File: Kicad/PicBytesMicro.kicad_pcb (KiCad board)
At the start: 2 copper layers, 80 x 125 mm, 274 parts, among them IC1 FS312F-G, Q1 SMMBT5551LT1G, Q10 SMMBT5551LT1G, Q11 SMMBT5551LT1G, Q12 SMMBT5551LT1G, Q13 SMMBT5551LT1G, Q14 SMMBT5551LT1G, Q15 SMMBT5551LT1G, Q16 SMMBT5551LT1G, Q17 SMMBT5551LT1G, Q18 SMMBT5551LT1G, Q19 SMMBT5551LT1G, Q2 SMMBT5551LT1G, Q20 SMMBT5551LT1G, Q21 SMMBT5551LT1G, Q22 SMMBT5551LT1G, Q23 SMMBT5551LT1G, Q24 SMMBT5551LT1G, Q25 SMMBT5551LT1G, Q26 SMMBT5551LT1G, Q27 SMMBT5551LT1G, Q28 SMMBT5551LT1G, Q29 SMMBT5551LT1G, Q3 SMMBT5551LT1G, Q30 FS8205, Q4 SMMBT5551LT1G, Q5 SMMBT5551LT1G, Q6 SMMBT5551LT1G, Q7 SMMBT5551LT1G, Q8 SMMBT5551LT1G, Q9 SMMBT5551LT1G

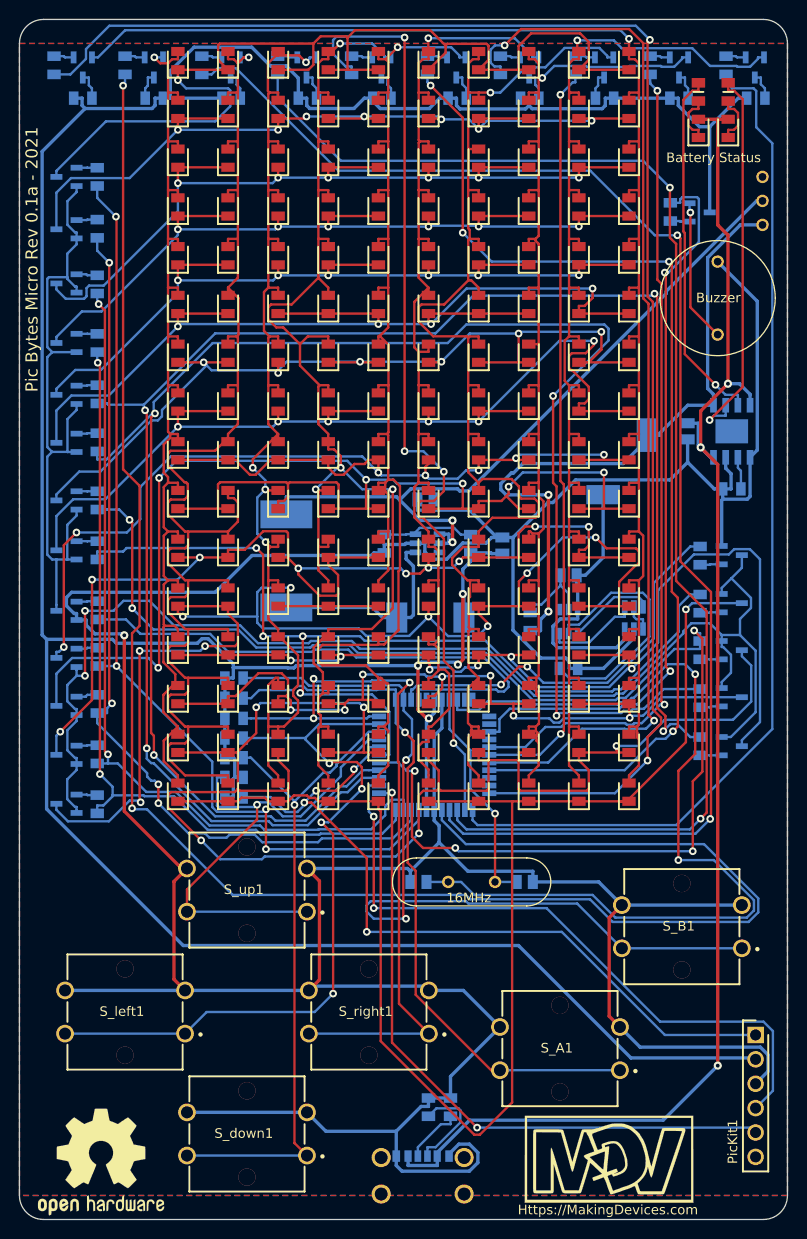
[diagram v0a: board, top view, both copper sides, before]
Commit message: New V1.2 Hardware Release
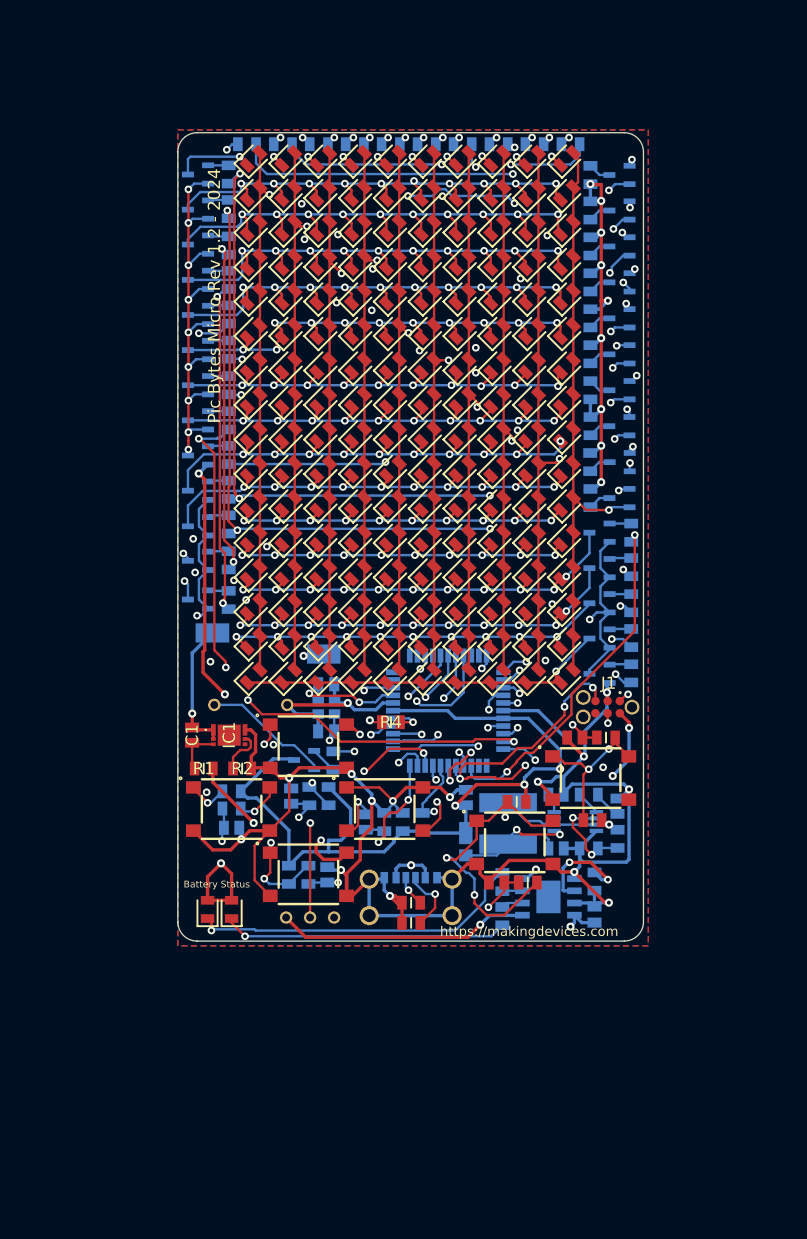
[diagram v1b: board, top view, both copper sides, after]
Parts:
- removed 16MhzCrystal1: AS-16.000MAHK-B, SamacSys_Parts:AS16000MAHKB
- removed C_0.1u_1, C_22u_1, C_22u_2: GCG21BR71H154KA01K, SamacSys_Parts:CAPC2012X145N
- removed D_1: SS34-E3_57T, SamacSys_Parts:DIOM7959X262N
- removed G***: LOGO, MDV:logo_MDV_2
- removed L_22uH_1: SRR1260-220M, SamacSys_Parts:SRR1260-150M
- removed PicKit1: M20-9990645, SamacSys_Parts:HDRV6W66P0X254_1X6_1524X254X874P
- removed Q30: FS8205, SamacSys_Parts:FS8205
- removed REF**: OSHW-Logo2_14.6x12mm_SilkScreen, Symbol:OSHW-Logo2_14.6x12mm_SilkScreen
- removed R_100_1, R_1k_3, R_2k_2, R_7.5k_1: KTR10EZPF4220, SamacSys_Parts:RESC2012X65N
- removed S_A1, S_B1: B3F-4050, SamacSys_Parts:B3F-4000
- removed U_StepUp1: MT3608, SamacSys_Parts:SOT95P280X145-6N
- added C1: 1uF, SamacSys_Parts:CAPC2012X140N, F.Cu at (114.5, 109.0)
- added C2: 820pF, User_lib:CAPC2012X140N, B.Cu at (158.8, 116.5)
- added C3: 22uF, User_lib:CAPC2012X140N, B.Cu at (152.4, 120.8)
- added C4: 100nF, User_lib:CAPC2012X140N, B.Cu at (152.4, 115.2)
- added C5: 47uF, User_lib:CAPC2012X140N, B.Cu at (143.0, 115.5)
- added C_100F_1: GCG21BR71H154KA01K, User_lib:CAPC2012X140N, B.Cu at (124.8, 115.4)
- added C_22p_3: GCG21BR71H154KA01K, User_lib:CAPC2012X140N, B.Cu at (118.6, 118.7)
- added C_22p_4: GCG21BR71H154KA01K, User_lib:CAPC2012X140N, B.Cu at (128.6, 123.6)
- added C_22p_5: GCG21BR71H154KA01K, User_lib:CAPC2012X140N, B.Cu at (132.6, 118.1)
- added C_22p_6: GCG21BR71H154KA01K, User_lib:CAPC2012X140N, F.Cu at (154.3, 109.3)
- added C_22p_7: GCG21BR71H154KA01K, User_lib:CAPC2012X140N, F.Cu at (146.2, 124.4)
- added D1: FSV360FP, User_lib:SS12FP, B.Cu at (143.0, 120.2)
- added IC2: TPS61085TDGKR, User_lib:SOP65P490X110-8N, B.Cu at (154.4, 118.0)
- added J1: TC2030-MCP-NL, User_lib:TC2030-MCP-NL, F.Cu at (157.8, 106.1)
- added L1: 4.7uH, User_lib:SRN6045_1, B.Cu at (147.4, 118.2)
- added R1: 330, SamacSys_Parts:RESC2012X75N, F.Cu at (115.7, 112.5)
- added R2: 2.7k, SamacSys_Parts:RESC2012X75N, F.Cu at (119.7, 112.5)
- added R3: 44.2k, User_lib:RESC2012X75N, B.Cu at (155.8, 115.2)
- added R4: 10k, SamacSys_Parts:RESC2012X75N, F.Cu at (135.2, 107.7)
- added R5: 82k, User_lib:RESC2012X75N, B.Cu at (158.8, 119.8)
- added R6: 27k, User_lib:RESC2012X75N, B.Cu at (155.8, 120.8)
- added R_10K_10: KTR10EZPF4220, User_lib:RESC2012X75N, F.Cu at (157.6, 109.3)
- added R_10K_11: KTR10EZPF4220, User_lib:RESC2012X75N, F.Cu at (149.4, 124.4)
- added R_10K_2: KTR10EZPF4220, User_lib:RESC2012X75N, B.Cu at (118.6, 116.7)
- added R_10K_4: KTR10EZPF4220, User_lib:RESC2012X75N, B.Cu at (126.6, 123.6)
- added R_10K_5: KTR10EZPF4220, User_lib:RESC2012X75N, B.Cu at (128.7, 115.4)
- added R_10K_8: KTR10EZPF4220, User_lib:RESC2012X75N, B.Cu at (134.5, 118.1)
- added S_a1: 430182050816, User_lib:430182070816, F.Cu at (148.1, 120.2)
- added S_b1: 430182050816, User_lib:430182070816, F.Cu at (156.0, 113.5)
- added Y1: CX2520DB12000D0GPSC1, User_lib:CX2520DB12000D0GPSC1, B.Cu at (128.5, 106.2)
- IC1: value FS312F-G -> AP9214L-AN-HSBR-7; footprint SamacSys_Parts:SOT95P280X145-6N -> SamacSys_Parts:AP9214LANHSBR7; moved to F.Cu
- LS1, R_1k_1, R_1k_2: moved to B.Cu
- R_10K_12: renamed from R_10K_5; moved to F.Cu
- R_10K_13: renamed from R_10K_6; moved to F.Cu
- R_5.1_1, R_5.1k_1: moved to F.Cu
- S_down1, S_left1, S_right1, S_up1: value B3F-4050 -> 430182050816; footprint SamacSys_Parts:B3F-4000 -> User_lib:430182070816
- moved LED_RED_bms1 96.4 mm to (118.6, 127.2)
- moved LED_Green_bms1 96.1 mm to (116.1, 127.2)
- moved R_1k_1 89.0 mm to (146.8, 127.9)
- moved SW_Toggle1 87.6 mm to (124.3, 128.1), turned to 0 degrees
- moved R_1k_2 84.8 mm to (146.8, 124.3), turned to 90 degrees
- moved Q27 71.7 mm to (159.0, 84.4), turned to 180 degrees
- moved Q1 70.4 mm to (126.2, 111.6), turned to 180 degrees
- moved R220_10 67.3 mm to (156.0, 84.4), turned to -90 degrees
- moved R4K7_1 67.1 mm to (129.2, 111.7)
- moved LS1 65.1 mm to (116.8, 105.9), turned to 90 degrees
- moved R4K7_27 54.4 mm to (153.9, 47.5), turned to 180 degrees
- moved IC_BMS_TP1 52.1 mm to (151.6, 125.9), turned to 180 degrees
- moved C_10u_1 51.3 mm to (156.4, 127.7), turned to 90 degrees
- moved Q4 49.8 mm to (159.0, 50.7), turned to 180 degrees
- moved R220_1 46.1 mm to (156.0, 50.7), turned to 90 degrees
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- renumbered IC_BMS_TP4056 to IC_BMS_TP1, PIC18F45K50 to PIC18F45K1, Q29 to Q1, Q9 to Q10, Q10 to Q11, Q11 to Q12, Q12 to Q13, Q13 to Q14, Q14 to Q15, Q15 to Q16, Q16 to Q17, Q17 to Q18, Q18 to Q19, Q1 to Q2, Q19 to Q20, Q20 to Q21, Q21 to Q22, Q22 to Q23, Q23 to Q24, Q24 to Q25, Q25 to Q26, Q26 to Q27, Q27 to Q28, Q28 to Q29, Q2 to Q3, Q3 to Q4, Q4 to Q5, Q5 to Q6, Q6 to Q7, Q7 to Q8, Q8 to Q9, R4K7_29 to R4K7_1, R4K7_9 to R4K7_10, R4K7_10 to R4K7_11, R4K7_11 to R4K7_12, R4K7_12 to R4K7_13, R4K7_13 to R4K7_14, R4K7_14 to R4K7_15, R4K7_15 to R4K7_16, R4K7_16 to R4K7_17, R4K7_17 to R4K7_18, R4K7_18 to R4K7_19, R4K7_1 to R4K7_2, R4K7_19 to R4K7_20, R4K7_20 to R4K7_21, R4K7_21 to R4K7_22, R4K7_22 to R4K7_23, R4K7_23 to R4K7_24, R4K7_24 to R4K7_25, R4K7_25 to R4K7_26, R4K7_26 to R4K7_27, R4K7_27 to R4K7_28, R4K7_28 to R4K7_29, R4K7_2 to R4K7_3, R4K7_3 to R4K7_4, R4K7_4 to R4K7_5, R4K7_5 to R4K7_6, R4K7_6 to R4K7_7, R4K7_7 to R4K7_8, R4K7_8 to R4K7_9, R_10K_1 to R_10K_3, R_10K_3 to R_10K_6, R_10K_2 to R_10K_7, R_10K_4 to R_10K_9
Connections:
- IC1 pad 1: Net-(IC1-Pad1) -> BAT-
- IC1 pad 2: Net-(IC1-Pad2) -> BAT-
- IC1 pad 4: Net-(IC1-Pad4) -> unconnected-(IC1-NC-Pad4)
- IC1 pad 6: BAT- -> Vgnd_main
- IC_BMS_TP1 pad 9: Net-(IC_BMS_TP4056-Pad9) -> unconnected-(IC_BMS_TP1-EP-Pad9)
- J_USB_C1 pad MH1: Net-(J_USB_C1-PadMH1) -> Vgnd_main
- J_USB_C1 pad MH2: Net-(J_USB_C1-PadMH2) -> Vgnd_main
- J_USB_C1 pad MH3: Net-(J_USB_C1-PadMH3) -> Vgnd_main
- J_USB_C1 pad MH4: Net-(J_USB_C1-PadMH4) -> Vgnd_main
- PIC18F45K1 pad 12: ICSPCLK -> unconnected-(PIC18F45K1-NC/ICCK/ICPGC-Pad12)
- PIC18F45K1 pad 13: ICSPDA -> unconnected-(PIC18F45K1-NC/ICDT/ICPGD-Pad13)
- PIC18F45K1 pad 16: P_CR6 -> ICSPCLK
- PIC18F45K1 pad 17: P_CR7 -> ICSPDA
- PIC18F45K1 pad 27: Net-(PIC18F45K50-Pad27) -> Vdc_battery
- PIC18F45K1 pad 32: Net-(PIC18F45K50-Pad32) -> unconnected-(PIC18F45K1-RC0-Pad32)
- PIC18F45K1 pad 33: Net-(PIC18F45K50-Pad33) -> unconnected-(PIC18F45K1-NC/~{ICRST}/ICVPP-Pad33)
- PIC18F45K1 pad 34: Net-(PIC18F45K50-Pad34) -> unconnected-(PIC18F45K1-NC-Pad34)
- PIC18F45K1 pad 35: Net-(PIC18F45K50-Pad35) -> unconnected-(PIC18F45K1-RC1-Pad35)
- PIC18F45K1 pad 37: Net-(PIC18F45K50-Pad37) -> unconnected-(PIC18F45K1-VUSB3V3-Pad37)
- PIC18F45K1 pad 42: Net-(PIC18F45K50-Pad42) -> unconnected-(PIC18F45K1-D--Pad42)
- PIC18F45K1 pad 43: Net-(PIC18F45K50-Pad43) -> unconnected-(PIC18F45K1-D+-Pad43)
- R4K7_24 pad 1: P_CR6 -> ICSPCLK
- R4K7_25 pad 1: P_CR6 -> ICSPCLK
- R4K7_28 pad 1: P_CR7 -> ICSPDA
- R4K7_29 pad 1: P_CR7 -> ICSPDA
- R_10K_12 pad 1: S_b -> Net-(R_10K_10-Pad2)
- R_10K_13 pad 1: S_a -> Net-(R_10K_11-Pad2)
- R_10K_3 pad 1: S_left -> Net-(R_10K_2-Pad2)
- R_10K_6 pad 1: S_up -> Net-(R_10K_5-Pad1)
- R_10K_6 pad 2: Vcc_main -> S_up
- R_10K_7 pad 1: S_down -> Net-(R_10K_4-Pad2)
- R_10K_9 pad 1: S_right -> Vgnd_main
- SW_Toggle1 pad 3: Net-(SW_Toggle1-Pad3) -> unconnected-(SW_Toggle1-Pad3)
- S_down1 pad 1: S_down -> Net-(R_10K_4-Pad2)
- S_down1 pad 2: S_down -> Vgnd_main
- S_down1 pad 3: Vgnd_main -> Net-(R_10K_4-Pad2)
- S_left1 pad 1: S_left -> Net-(R_10K_2-Pad2)
- S_left1 pad 2: S_left -> Vgnd_main
- S_left1 pad 3: Vgnd_main -> Net-(R_10K_2-Pad2)
- S_right1 pad 1: S_right -> Vgnd_main
- S_right1 pad 2: S_right -> Net-(C_22p_5-Pad2)
- S_right1 pad 4: Vgnd_main -> Net-(C_22p_5-Pad2)
- S_up1 pad 1: S_up -> Net-(R_10K_5-Pad1)
- S_up1 pad 2: S_up -> Vgnd_main
- S_up1 pad 3: Vgnd_main -> Net-(R_10K_5-Pad1)
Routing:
- net Vcc_main: track 360.6 -> 183.0 mm, vias 4 -> 15
- net Vgnd_main: track 425.9 -> 264.1 mm, vias 1 -> 17
- net P_CR6: track 145.7 -> 0.00 mm, vias 6 -> 0
- net R15: track 147.4 -> 38.9 mm
- net P_CR7: track 102.3 -> 0.00 mm, vias 4 -> 0
- net C10: track 162.2 -> 60.8 mm
- net R14: track 153.1 -> 52.6 mm, vias 5 -> 10
- net P_CC1: track 187.0 -> 86.8 mm
- net P_CC10: track 159.6 -> 65.1 mm
- net BMS_Vcc: track 151.8 -> 63.1 mm, vias 3 -> 4
- net R11: track 140.2 -> 56.4 mm, vias 9 -> 12
- net R9: track 138.2 -> 55.8 mm, vias 6 -> 10
- net Net-(PIC18F45K1-RA6): track 95.2 -> 13.7 mm
- net P_CR5: track 184.2 -> 107.7 mm
- net P_CR4: track 179.8 -> 108.7 mm
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- added copper zone on In1.Cu, net Vgnd_main
- added copper zone on In2.Cu, net Vgnd_main
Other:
- board size 80 x 125 mm -> 48.5 x 84.2 mm
- copper layers 2 -> 4
- board text added: "Pic Bytes Micro Rev 1.2 - 2024"
- board text added: "https://makingdevices.com"
- board text removed: "16MHz"
- board text removed: "FS312"
- board text removed: "Https://MakingDevices.com"
- board text removed: "MT3608"
- board text removed: "Pic Bytes Micro Rev 0.1a - 2021"
- board text removed: "R10K"
- board text removed: "R4K7"
- board text removed: "R5K1"
- board text removed: "TP4056"
- board text removed: "Type C"

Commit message: V1.25 FW release
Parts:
- renumbered LED_Green_bms1 to LED_Red_bms1, LED_RED_bms1 to LED_green_bms1
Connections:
- C_22p_5 pad 2: Net-(C_22p_5-Pad2) -> Vgnd_main
- R_10K_8 pad 2: Vgnd_main -> Net-(R_10K_8-Pad2)
- R_10K_9 pad 1: Vgnd_main -> Net-(R_10K_8-Pad2)
- S_right1 pad 1: Vgnd_main -> Net-(R_10K_8-Pad2)
- S_right1 pad 2: Net-(C_22p_5-Pad2) -> Vgnd_main
- S_right1 pad 3: Vgnd_main -> Net-(R_10K_8-Pad2)
- S_right1 pad 4: Net-(C_22p_5-Pad2) -> Vgnd_main
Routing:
- net Net-(C_22p_5-Pad2): track 17.9 -> 0.00 mm, vias 2 -> 0
- net Net-(R_10K_8-Pad2): track 0.00 -> 14.3 mm, vias 0 -> 1
- net Vgnd_main: track 264.1 -> 250.3 mm

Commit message: New HW v1.25 release
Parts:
- IC1: value AP9214L-AN-HSBR-7 -> AP9214L-AD-HSBR-7
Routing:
- net Vgnd_main: track 250.3 -> 250.9 mm
- net S_down: track 24.7 -> 25.2 mm
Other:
- board text added: "Pic Bytes Micro Rev 1.25 - 2024"
- board text removed: "Pic Bytes Micro Rev 1.2 - 2024"
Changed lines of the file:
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@@
         (effects (font (size 1.27 1.27) (thickness 0.254)))
     )
-    (fp_text value "AP9214L-AN-HSBR-7" (at 3.475 2 90) (layer "F.SilkS") hide
+    (fp_text value "AP9214L-AD-HSBR-7" (at 3.475 2 90) (layer "F.SilkS") hide
         (effects (font (size 1.27 1.27) (thickness 0.254)))
     )
@@
     (property "ki_description" "Power Inductor semi-shielded SMD 4.7uH Bourns SRN6045 Series Shielded Wire-wound SMD Inductor with a Ferrite Core, 4.7 uH +/-30% 4A Idc")
     (attr smd)
-    (fp_text reference "L1" (at -0.327 0.037 90) (layer "B.SilkS")
+    (fp_text reference "L1" (at -0.327 0.037 90) (layer "B.SilkS") hide
         (effects (font (size 1.27 1.27) (thickness 0.254)) (justify mirror))
     )
@@
     (property "ki_description" "Cap Ceramic 4.7uF 10V X7R 20% Pad SMD 0805 125C T/R")
     (attr smd)
-    (fp_text reference "C5" (at 0 0 -270) (layer "B.SilkS")
+    (fp_text reference "C5" (at 0 0 -270) (layer "B.SilkS") hide
         (effects (font (size 1.27 1.27) (thickness 0.254)) (justify mirror))
     )
@@
     (property "ki_description" "Schottky Diodes & Rectifiers 60V 3A Schottky Barrier Rectifier")
     (attr smd)
-    (fp_text reference "D1" (at -0.225 0 -270) (layer "B.SilkS")
+    (fp_text reference "D1" (at -0.225 0 -270) (layer "B.SilkS") hide
         (effects (font (size 1.27 1.27) (thickness 0.254)) (justify mirror))
     )
@@
     (property "ki_description" "Crystals AEC-Q200 12MHz 8pF 2.5x2mm")
     (attr smd)
-    (fp_text reference "Y1" (at -0.225 0) (layer "B.SilkS")
+    (fp_text reference "Y1" (at -0.225 0) (layer "B.SilkS") hide
         (effects (font (size 1.27 1.27) (thickness 0.254)) (justify mirror))
     )
@@
     (effects (font (size 1 1) (thickness 0.25)))
   )
-  (gr_text "Pic Bytes Micro Rev 1.2 - 2024" (at 116.8 63.3 90) (layer "F.SilkS")
+  (gr_text "Pic Bytes Micro Rev 1.25 - 2024" (at 116.8 63.3 90) (layer "F.SilkS")
     (effects (font (size 1.27 1.27) (thickness 0.15)))
   )
@@
   (segment (start 121 120.575) (end 122.575 119) (width 0.25) (layer "F.Cu") (net 5))
   (segment (start 145.4 124.4) (end 144.478618 123.478618) (width 0.35) (layer "F.Cu") (net 5))
+  (segment (start 140.325 117.675) (end 140.7 117.3) (width 0.35) (layer "F.Cu") (net 5))
   (segment (start 130 123.1) (end 130.575 123.675) (width 0.35) (layer "F.Cu") (net 5))
   (segment (start 147.515 122.1) (end 145.4 124.215) (width 0.35) (layer "F.Cu") (net 5))
@@
   (segment (start 140.325 117.7) (end 139.025 119) (width 0.25) (layer "F.Cu") (net 5))
   (segment (start 130.575 125.79273) (end 131.18727 125.79273) (width 0.35) (layer "F.Cu") (net 5))
+  (segment (start 140.7 117.3) (end 140.7 116.7) (width 0.35) (layer "F.Cu") (net 5))
   (segment (start 135.65 125.8) (end 136.35 126.5) (width 0.35) (layer "F.Cu") (net 5))
-  (segment (start 140.325 116.325) (end 140.325 117.7) (width 0.25) (layer "F.Cu") (net 5))
   (segment (start 136.35 127.05) (end 135.1 125.8) (width 0.35) (layer "F.Cu") (net 5))
   (segment (start 153.55 109.525) (end 155.296365 111.271365) (width 0.35) (layer "F.Cu") (net 5))
+  (segment (start 140.7 116.7) (end 140.325 116.325) (width 0.35) (layer "F.Cu") (net 5))
   (segment (start 122.625 112.45) (end 120.725 112.45) (width 0.35) (layer "F.Cu") (net 5))
   (segment (start 154.3 123.3) (end 157.5 126.5) (width 0.35) (layer "F.Cu") (net 5))
@@
   (segment (start 160 115.74643) (end 159.975065 115.771365) (width 0.35) (layer "F.Cu") (net 5))
   (segment (start 120.6 108.5) (end 120 108.5) (width 0.35) (layer "F.Cu") (net 5))
+  (segment (start 140.325 117.7) (end 140.325 117.675) (width 0.35) (layer "F.Cu") (net 5))
   (segment (start 115.1755 81.8) (end 115.8 82.4245) (width 0.35) (layer "F.Cu") (net 5))
   (segment (start 130.575 125) (end 130.575 125.79273) (width 0.35) (layer "F.Cu") (net 5))
@@
   (segment (start 124.6 106.1) (end 124.4 105.9) (width 0.35) (layer "In1.Cu") (net 5))
   (segment (start 123.125 104.625) (end 124.4 105.9) (width 0.35) (layer "In2.Cu") (net 5))
+  (segment (start 132.6255 115.15) (end 131.7755 116) (width 0.35) (layer "In2.Cu") (net 5))
+  (segment (start 132.9755 114.8) (end 132.6255 115.15) (width 0.35) (layer "In2.Cu") (net 5))
+  (segment (start 139.15 115.15) (end 140 116) (width 0.35) (layer "In2.Cu") (net 5))
   (segment (start 117.9 104.8) (end 118.075 104.625) (width 0.35) (layer "In2.Cu") (net 5))
-  (segment (start 139.15 115.15) (end 140 116) (width 0.25) (layer "In2.Cu") (net 5))
-  (segment (start 131.7755 116) (end 132.6255 115.15) (width 0.25) (layer "In2.Cu") (net 5))
-  (segment (start 132.6255 115.15) (end 139.15 115.15) (width 0.25) (layer "In2.Cu") (net 5))
+  (segment (start 138.8 114.8) (end 132.9755 114.8) (width 0.35) (layer "In2.Cu") (net 5))
+  (segment (start 139.15 115.15) (end 138.8 114.8) (width 0.35) (layer "In2.Cu") (net 5))
   (segment (start 118.075 104.625) (end 123.125 104.625) (width 0.35) (layer "In2.Cu") (net 5))
   (segment (start 119.6 119.9) (end 119.6 118.7) (width 0.35) (layer "B.Cu") (net 5))
@@
   (via (at 129.7 124.4) (size 0.8) (drill 0.4) (layers "F.Cu" "B.Cu") (net 70))
   (via (at 138.602551 110.911981) (size 0.8) (drill 0.4) (layers "F.Cu" "B.Cu") (net 70))
-  (segment (start 129.760661 124.4) (end 129.7 124.4) (width 0.25) (layer "In1.Cu") (net 70))
-  (segment (start 132.4 112.8) (end 132.4 121.760661) (width 0.25) (layer "In1.Cu") (net 70))
-  (segment (start 132.4 121.760661) (end 129.760661 124.4) (width 0.25) (layer "In1.Cu") (net 70))
+  (segment (start 129.760661 124.4) (end 132.5005 121.660161) (width 0.25) (layer "In1.Cu") (net 70))
+  (segment (start 133.1 118.7) (end 133.1 113.5) (width 0.25) (layer "In1.Cu") (net 70))
+  (segment (start 133.1 113.5) (end 132.4 112.8) (width 0.25) (layer "In1.Cu") (net 70))
+  (segment (start 129.7 124.4) (end 129.760661 124.4) (width 0.25) (layer "In1.Cu") (net 70))
+  (segment (start 132.5005 121.660161) (end 132.5005 119.2995) (width 0.25) (layer "In1.Cu") (net 70))
+  (segment (start 132.5005 119.2995) (end 133.1 118.7) (width 0.25) (layer "In1.Cu") (net 70))
   (segment (start 126.75 124.4) (end 126.6 124.55) (width 0.25) (layer "B.Cu") (net 70))
   (segment (start 129.7 124.4) (end 128.57 124.4) (width 0.25) (layer "B.Cu") (net 70))
@@
   (via (at 125.6 117.6) (size 0.8) (drill 0.4) (layers "F.Cu" "B.Cu") (net 71))
   (via (at 139.9 113.7) (size 0.8) (drill 0.4) (layers "F.Cu" "B.Cu") (net 71))
-  (segment (start 139.9 113.7) (end 139 114.6) (width 0.25) (layer "In2.Cu") (net 71))
-  (segment (start 127.8 114.6) (end 125.6 116.8) (width 0.25) (layer "In2.Cu") (net 71))
-  (segment (start 139 114.6) (end 127.8 114.6) (width 0.25) (layer "In2.Cu") (net 71))
-  (segment (start 125.6 116.8) (end 125.6 117.6) (width 0.25) (layer "In2.Cu") (net 71))
+  (segment (start 125.6 116.8) (end 128.1 114.3) (width 0.25) (layer "In2.Cu") (net 71))
+  (segment (start 139.9 113.7) (end 139.35 114.25) (width 0.25) (layer "In2.Cu") (net 71))
+  (segment (start 139.3 114.3) (end 139.35 114.25) (width 0.25) (layer "In2.Cu") (net 71))
+  (segment (start 125.6 117.6) (end 125.6 116.8) (width 0.25) (layer "In2.Cu") (net 71))
+  (segment (start 128.1 114.3) (end 139.3 114.3) (width 0.25) (layer "In2.Cu") (net 71))
   (segment (start 139.562 113.362) (end 139.9 113.7) (width 0.25) (layer "B.Cu") (net 71))
   (segment (start 126.55 116.2) (end 126.7 116.35) (width 0.25) (layer "B.Cu") (net 71))

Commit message: Bill Of Materials
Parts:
- C10: renamed from C_22p_6; value GCG21BR71H154KA01K -> 100nF
- C11: renamed from C_22p_7; value GCG21BR71H154KA01K -> 100nF
- C12: renamed from C_22p_1; value GCG21BR71H154KA01K -> 22pF
- C13: renamed from C_22p_2; value GCG21BR71H154KA01K -> 22pF
- C14: renamed from C_10u_1; value GCG21BR71H154KA01K -> 10uF
- C6: renamed from C_22p_3; value GCG21BR71H154KA01K -> 100nF
- C7: renamed from C_22p_4; value GCG21BR71H154KA01K -> 100nF
- C8: renamed from C_100F_1; value GCG21BR71H154KA01K -> 100nF
- C9: renamed from C_22p_5; value GCG21BR71H154KA01K -> 100nF
- PIC18F4550: renamed from PIC18F45K1; value PIC18F45K50-I_PT -> PIC18F4550-I_PT
- R10: renamed from R4K7_4; value KTR10EZPF4220 -> 4k7
- R11: renamed from R4K7_5; value KTR10EZPF4220 -> 4k7
- R12: renamed from R4K7_6; value KTR10EZPF4220 -> 4k7
- R13: renamed from R4K7_7; value KTR10EZPF4220 -> 4k7
- R14: renamed from R220_1; value KTR10EZPF4220 -> 220
- R15: renamed from R220_2; value KTR10EZPF4220 -> 220
- R16: renamed from R4K7_8; value KTR10EZPF4220 -> 4k7
- R17: renamed from R4K7_9; value KTR10EZPF4220 -> 4k7
- R18: renamed from R4K7_10; value KTR10EZPF4220 -> 4k7
- R19: renamed from R4K7_11; value KTR10EZPF4220 -> 4k7
- R20: renamed from R220_3; value KTR10EZPF4220 -> 220
- R21: renamed from R220_4; value KTR10EZPF4220 -> 220
- R22: renamed from R4K7_12; value KTR10EZPF4220 -> 4k7
- R220: renamed from R220_8; value KTR10EZPF4220 -> 220
- R23: renamed from R4K7_13; value KTR10EZPF4220 -> 4k7
- R24: renamed from R4K7_14; value KTR10EZPF4220 -> 4k7
- R25: renamed from R4K7_15; value KTR10EZPF4220 -> 4k7
- R26: renamed from R4K7_16; value KTR10EZPF4220 -> 4k7
- R27: renamed from R4K7_17; value KTR10EZPF4220 -> 4k7
- R28: renamed from R4K7_18; value KTR10EZPF4220 -> 4k7
- R29: renamed from R4K7_19; value KTR10EZPF4220 -> 4k7
- R30: renamed from R220_5; value KTR10EZPF4220 -> 220
- R31: renamed from R220_6; value KTR10EZPF4220 -> 220
- R32: renamed from R4K7_20; value KTR10EZPF4220 -> 4k7
- R33: renamed from R4K7_21; value KTR10EZPF4220 -> 4k7
- R34: renamed from R4K7_22; value KTR10EZPF4220 -> 4k7
- R35: renamed from R4K7_23; value KTR10EZPF4220 -> 4k7
- R36: renamed from R220_7; value KTR10EZPF4220 -> 220
- R37: renamed from R4K7_24; value KTR10EZPF4220 -> 4k7
- R38: renamed from R4K7_25; value KTR10EZPF4220 -> 4k7
- R39: renamed from R4K7_26; value KTR10EZPF4220 -> 4k7
- R40: renamed from R4K7_27; value KTR10EZPF4220 -> 4k7
- R41: renamed from R220_9; value KTR10EZPF4220 -> 220
- R42: renamed from R220_10; value KTR10EZPF4220 -> 220
- R43: renamed from R4K7_28; value KTR10EZPF4220 -> 4k7
- R44: renamed from R4K7_29; value KTR10EZPF4220 -> 4k7
- R45: renamed from R_10k_1; value KTR10EZPF4220 -> 10k
- R46: renamed from R_10K_2; value KTR10EZPF4220 -> 10k
- R47: renamed from R_10K_3; value KTR10EZPF4220 -> 10k
- R48: renamed from R_10K_4; value KTR10EZPF4220 -> 10k
- R49: renamed from R_10K_5; value KTR10EZPF4220 -> 10k
- R50: renamed from R_10K_6; value KTR10EZPF4220 -> 10k
- R51: renamed from R_10K_7; value KTR10EZPF4220 -> 10k
- R52: renamed from R_10K_8; value KTR10EZPF4220 -> 10k
- R53: renamed from R_10K_9; value KTR10EZPF4220 -> 10k
- R54: renamed from R_10K_10; value KTR10EZPF4220 -> 10k
- R55: renamed from R_10K_11; value KTR10EZPF4220 -> 10k
- R56: renamed from R_10K_12; value KTR10EZPF4220 -> 10k
- R57: renamed from R_10K_13; value KTR10EZPF4220 -> 10k
- R58: renamed from R_2k_1; value KTR10EZPF4220 -> 2k
- R59: renamed from R_1k_1; value KTR10EZPF4220 -> 1k
- R60: renamed from R_1k_2; value KTR10EZPF4220 -> 1k
- R61: renamed from R_5.1k_1; value KTR10EZPF4220 -> 5.1k
- R62: renamed from R_5.1_1; value KTR10EZPF4220 -> 5.1k
- R7: renamed from R4K7_1; value KTR10EZPF4220 -> 4k7
- R8: renamed from R4K7_2; value KTR10EZPF4220 -> 4k7
- R9: renamed from R4K7_3; value KTR10EZPF4220 -> 4k7
